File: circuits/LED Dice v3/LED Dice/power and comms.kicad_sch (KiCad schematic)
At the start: 13 parts, among them J1 KH-TYPE-C-16P, J3 Conn_01x02_Pin, SW1 SW_SPDT, U3 TP4057, U4 LTST-C195KGJRKT, U5 TLV74333PDBVR, U6 MT3608

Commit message: schematic is complete
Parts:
- added C10, C9: 100 nF, Capacitor_SMD:C_0603_1608Metric_Pad1.08x0.95mm_HandSolder, symbol Device:C
- added C11, C12, C8: 10 uF, symbol Device:C
- added C7: 1 uF, symbol Device:C
- added D15: SS115, Diode_SMD:D_SMA_Handsoldering, symbol Device:D_Schottky
- added L1: 6.8 uH, Inductor_SMD:L_Coilcraft_XxL4020, symbol Device:L
- added R10, R9: 5.1k, Resistor_SMD:R_0603_1608Metric_Pad0.98x0.95mm_HandSolder, symbol Device:R
- added R7: 110 k, symbol Device:R
- added R8: 15 k, symbol Device:R
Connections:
- net Batt+: now also R9.1
- net GND: now also U6.2 (GND), C10.2, C11.2, C12.2, C7.2, C8.2, C9.2, R10.2, R8.2
- net VBatt+: now also U6.4 (EN), U6.5 (IN), C7.1, C8.1, C9.1, L1.1
- net at U6.1 (SW): now also D15.2 (A), L1.2
- net Vfb: now reaches U6.3 (FB)
- net Vfb: now also R7.2, R8.1
- net D+ renamed USB D+
- net D- renamed USB D-
- new net +5V: C10.1, C11.1, C12.1, D15.1 (K), R7.1
- new net Vsense: R10.1, R9.2
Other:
- note added: "5V Boost Converter"
- note added: "Battery Voltage Feedback"
- moved on the sheet: C6, U5, U6

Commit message: layout progress
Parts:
- removed SW1: SW_SPDT, Button_Switch_SMD:SW_SPDT_Shouhan_MSK12C02, symbol Switch:SW_SPDT
- added S1: 450404015514, SMD slide switch:450404015514, symbol 450404015514:450404015514
- C11, C7: footprint (none) -> Capacitor_SMD:C_0805_2012Metric_Pad1.18x1.45mm_HandSolder
- C12, C8: footprint (none) -> Capacitor_SMD:C_1206_3216Metric_Pad1.33x1.80mm_HandSolder
- J1: footprint Connector_PinHeader_2.54mm:PinHeader_1x04_P2.54mm_Vertical -> Connector_USB:USB_C_Receptacle_GCT_USB4105-xx-A_16P_TopMnt_Horizontal
- L1: footprint Inductor_SMD:L_Coilcraft_XxL4020 -> Inductor_SMD:L_Changjiang_FXL0412
- R7, R8: footprint (none) -> Resistor_SMD:R_0603_1608Metric_Pad0.98x0.95mm_HandSolder
- U3: Part No (none) -> TP4057
- U4: footprint LTST-C195KGJRKT:LTST-BILED-15X16 -> LEDs:LTST-BILED-15X16
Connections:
- net Batt+: now also S1.2
- net VBatt+: now also S1.3
- net Vbus: now also U4.P$1, U4.P$2; no longer R4.1, R5.1
- net at R5.2: now also U3.5 (STDBY); no longer U4.P$1
- net at R4.2: now also U3.1 (~{CHRG}); no longer U4.P$2
- net at U4.P$3: now also R5.1; no longer U3.5 (STDBY)
- net at U4.P$4: now also R4.1; no longer U3.1 (~{CHRG})
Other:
- moved on the sheet: R4, R5

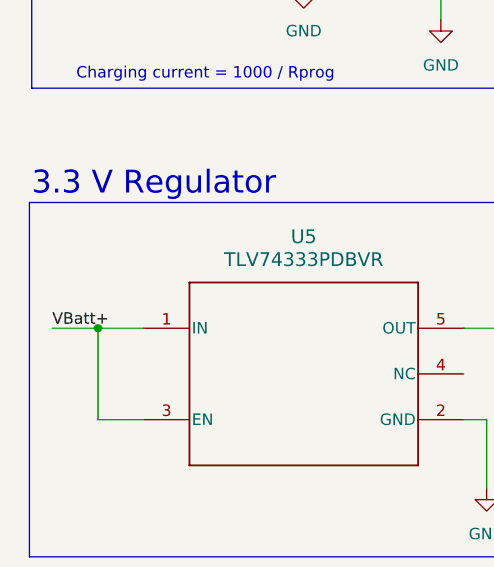
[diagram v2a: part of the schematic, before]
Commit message: layout complete, some DRC violations are present
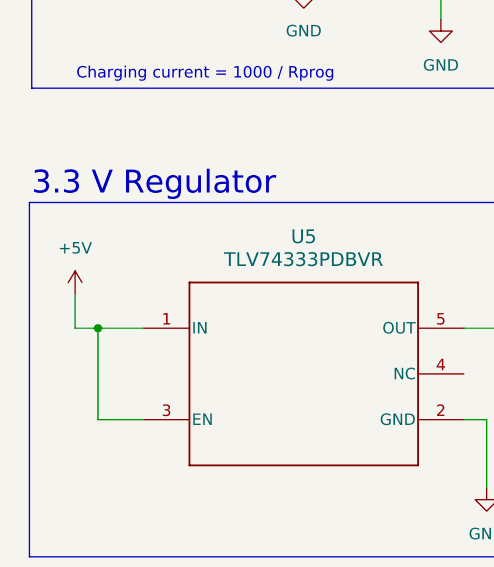
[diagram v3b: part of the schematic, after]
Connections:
- net +5V: now also U5.1 (IN), U5.3 (EN)
- net VBatt+: no longer U5.1 (IN), U5.3 (EN)
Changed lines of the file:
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@@
+	)
+	(junction
+		(at 170.18 125.73)
+		(diameter 0)
+		(color 0 0 0 0)
+	)
+	(junction
+		(at 172.72 125.73)
+		(diameter 0)
+		(color 0 0 0 0)
+	)
+	(junction
+		(at 231.14 125.73)
+		(diameter 0)
+		(color 0 0 0 0)
+	)
+	(junction
+		(at 156.21 66.04)
+		(diameter 0)
+		(color 0 0 0 0)
+	)
+	(junction
+		(at 95.25 163.83)
+		(diameter 0)
+		(color 0 0 0 0)
 	)
 	(junction
@@
 	)
 	(junction
-		(at 170.18 125.73)
-		(diameter 0)
-		(color 0 0 0 0)
-	)
-	(junction
-		(at 172.72 125.73)
-		(diameter 0)
-		(color 0 0 0 0)
-	)
-	(junction
-		(at 231.14 125.73)
-		(diameter 0)
-		(color 0 0 0 0)
-	)
-	(junction
-		(at 156.21 66.04)
-		(diameter 0)
-		(color 0 0 0 0)
-	)
-	(junction
-		(at 95.25 163.83)
-		(diameter 0)
-		(color 0 0 0 0)
-	)
-	(junction
 		(at 259.08 127)
 		(diameter 0)
@@
 	(wire
 		(pts
-			(xy 34.29 163.83) (xy 39.37 163.83)
+			(xy 36.83 163.83) (xy 39.37 163.83)
 		)
 		(stroke
@@
 		(pts
 			(xy 66.04 45.72) (xy 71.12 45.72)
+		)
+		(stroke
+			(width 0)
+			(type default)
+		)
+	)
+	(wire
+		(pts
+			(xy 36.83 163.83) (xy 36.83 160.02)
 		)
 		(stroke
@@
 			)
 			(justify right bottom)
-		)
-	)
-	(label "VBatt+"
-		(at 34.29 163.83 0)
-		(effects
-			(font
-				(size 1.27 1.27)
-			)
-			(justify left bottom)
 		)
 	)
@@
 					(unit 1)
 				)
+			)
+		)
+	)
+	(symbol
+		(lib_id "power:+5V")
+		(at 36.83 160.02 0)
+		(unit 1)
+		(body_style 1)
+		(exclude_from_sim no)
+		(in_bom yes)
+		(on_board yes)
+		(in_pos_files yes)
+		(dnp no)
+		(fields_autoplaced yes)
+		(property "Reference" "#PWR081"
+			(at 36.83 163.83 0)
+			(hide yes)
+			(show_name no)
+			(do_not_autoplace no)
+			(effects
+				(font
+					(size 1.27 1.27)
+				)
+			)
+		)
+		(property "Value" "+5V"
+			(at 36.83 154.94 0)
+			(show_name no)
+			(do_not_autoplace no)
+			(effects
+				(font
+					(size 1.27 1.27)
+				)
+			)
+		)
+		(property "Footprint" ""
+			(at 36.83 160.02 0)
+			(hide yes)
+			(show_name no)
+			(do_not_autoplace no)
+			(effects
+				(font
+					(size 1.27 1.27)
+				)
+			)
+		)
+		(property "Datasheet" ""
+			(at 36.83 160.02 0)
+			(hide yes)
+			(show_name no)
+			(do_not_autoplace no)
+			(effects
+				(font
+					(size 1.27 1.27)
+				)
+			)
+		)
+		(property "Description" "Power symbol creates a global label with name \"+5V\""
+			(at 36.83 160.02 0)
+			(hide yes)
+			(show_name no)
+			(do_not_autoplace no)
+			(effects
+				(font
+					(size 1.27 1.27)
+				)
+			)
+		)
+		(pin "1"
+		)
+		(instances
+			(project "LED Dice"
+				(path "/ee819b49-61a1-4f22-8cb6-332b1c3be766/7600acdb-6a32-495d-b4cf-494d3fc1093a"
+					(reference "#PWR081")
+					(unit 1)
+				)
